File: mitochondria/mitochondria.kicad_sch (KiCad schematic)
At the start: 0 parts

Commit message: Started BMS with BQ77915 for 4S Battery design
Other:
- added sheet Battery Management (bms.kicad_sch)
- added sheet Connectors (conn.kicad_sch)
- added sheet Power Distribution (pd.kicad_sch)
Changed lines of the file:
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@@
 	(generator_version "9.0")
 	(paper "A4")
+	(sheet
+		(at 115.57 16.51)
+		(size 95.25 69.85)
+		(exclude_from_sim no)
+		(in_bom yes)
+		(on_board yes)
+		(dnp no)
+		(fields_autoplaced yes)
+		(stroke
+			(width 0.1524)
+			(type solid)
+		)
+		(fill
+			(color 0 0 0 0.0000)
+		)
+		(property "Sheetname" "Connectors"
+			(at 115.57 15.7984 0)
+			(effects
+				(font
+					(size 1.27 1.27)
+				)
+				(justify left bottom)
+			)
+		)
+		(property "Sheetfile" "conn.kicad_sch"
+			(at 115.57 86.9446 0)
+			(effects
+				(font
+					(size 1.27 1.27)
+				)
+				(justify left top)
+			)
+		)
+		(property "Field2" ""
+			(at 115.57 16.51 0)
+			(effects
+				(font
+					(size 1.27 1.27)
+				)
+				(hide yes)
+			)
+		)
+		(instances
+			(project "mitochondria"
+				(path "/d5881702-98ec-4aea-8d9c-3c163ba85aa3"
+					(page "3")
+				)
+			)
+		)
+	)
+	(sheet
+		(at 17.78 92.71)
+		(size 92.71 68.58)
+		(exclude_from_sim no)
+		(in_bom yes)
+		(on_board yes)
+		(dnp no)
+		(fields_autoplaced yes)
+		(stroke
+			(width 0.1524)
+			(type solid)
+		)
+		(fill
+			(color 0 0 0 0.0000)
+		)
+		(property "Sheetname" "Battery Management"
+			(at 17.78 91.9984 0)
+			(effects
+				(font
+					(size 1.27 1.27)
+				)
+				(justify left bottom)
+			)
+		)
+		(property "Sheetfile" "bms.kicad_sch"
+			(at 17.78 161.8746 0)
+			(effects
+				(font
+					(size 1.27 1.27)
+				)
+				(justify left top)
+			)
+		)
+		(pin "CELL_0" input
+			(at 110.49 100.33 0)
+			(effects
+				(font
+					(size 1.27 1.27)
+				)
+				(justify right)
+			)
+		)
+		(pin "CELL_1" input
+			(at 110.49 104.14 0)
+			(effects
+				(font
+					(size 1.27 1.27)
+				)
+				(justify right)
+			)
+		)
+		(pin "CELL_2" input
+			(at 110.49 107.95 0)
+			(effects
+				(font
+					(size 1.27 1.27)
+				)
+				(justify right)
+			)
+		)
+		(pin "CELL_3" input
+			(at 110.49 111.76 0)
+			(effects
+				(font
+					(size 1.27 1.27)
+				)
+				(justify right)
+			)
+		)
+		(instances
+			(project "mitochondria"
+				(path "/d5881702-98ec-4aea-8d9c-3c163ba85aa3"
+					(page "4")
+				)
+			)
+		)
+	)
+	(sheet
+		(at 17.78 16.51)
+		(size 92.71 69.85)
+		(exclude_from_sim no)
+		(in_bom yes)
+		(on_board yes)
+		(dnp no)
+		(fields_autoplaced yes)
+		(stroke
+			(width 0.1524)
+			(type solid)
+		)
+		(fill
+			(color 0 0 0 0.0000)
+		)
+		(property "Sheetname" "Power Distribution"
+			(at 17.78 15.7984 0)
+			(effects
+				(font
+					(size 1.27 1.27)
+				)
+				(justify left bottom)
+			)
+		)
+		(property "Sheetfile" "pd.kicad_sch"
+			(at 17.78 86.9446 0)
+			(effects
+				(font
+					(size 1.27 1.27)
+				)
+				(justify left top)
+			)
+		)
+		(property "Field2" ""
+			(at 17.78 16.51 0)
+			(effects
+				(font
+					(size 1.27 1.27)
+				)
+			)
+		)
+		(instances
+			(project "mitochondria"
+				(path "/d5881702-98ec-4aea-8d9c-3c163ba85aa3"
+					(page "2")
+				)
+			)
+		)
+	)
 	(sheet_instances
 		(path "/"

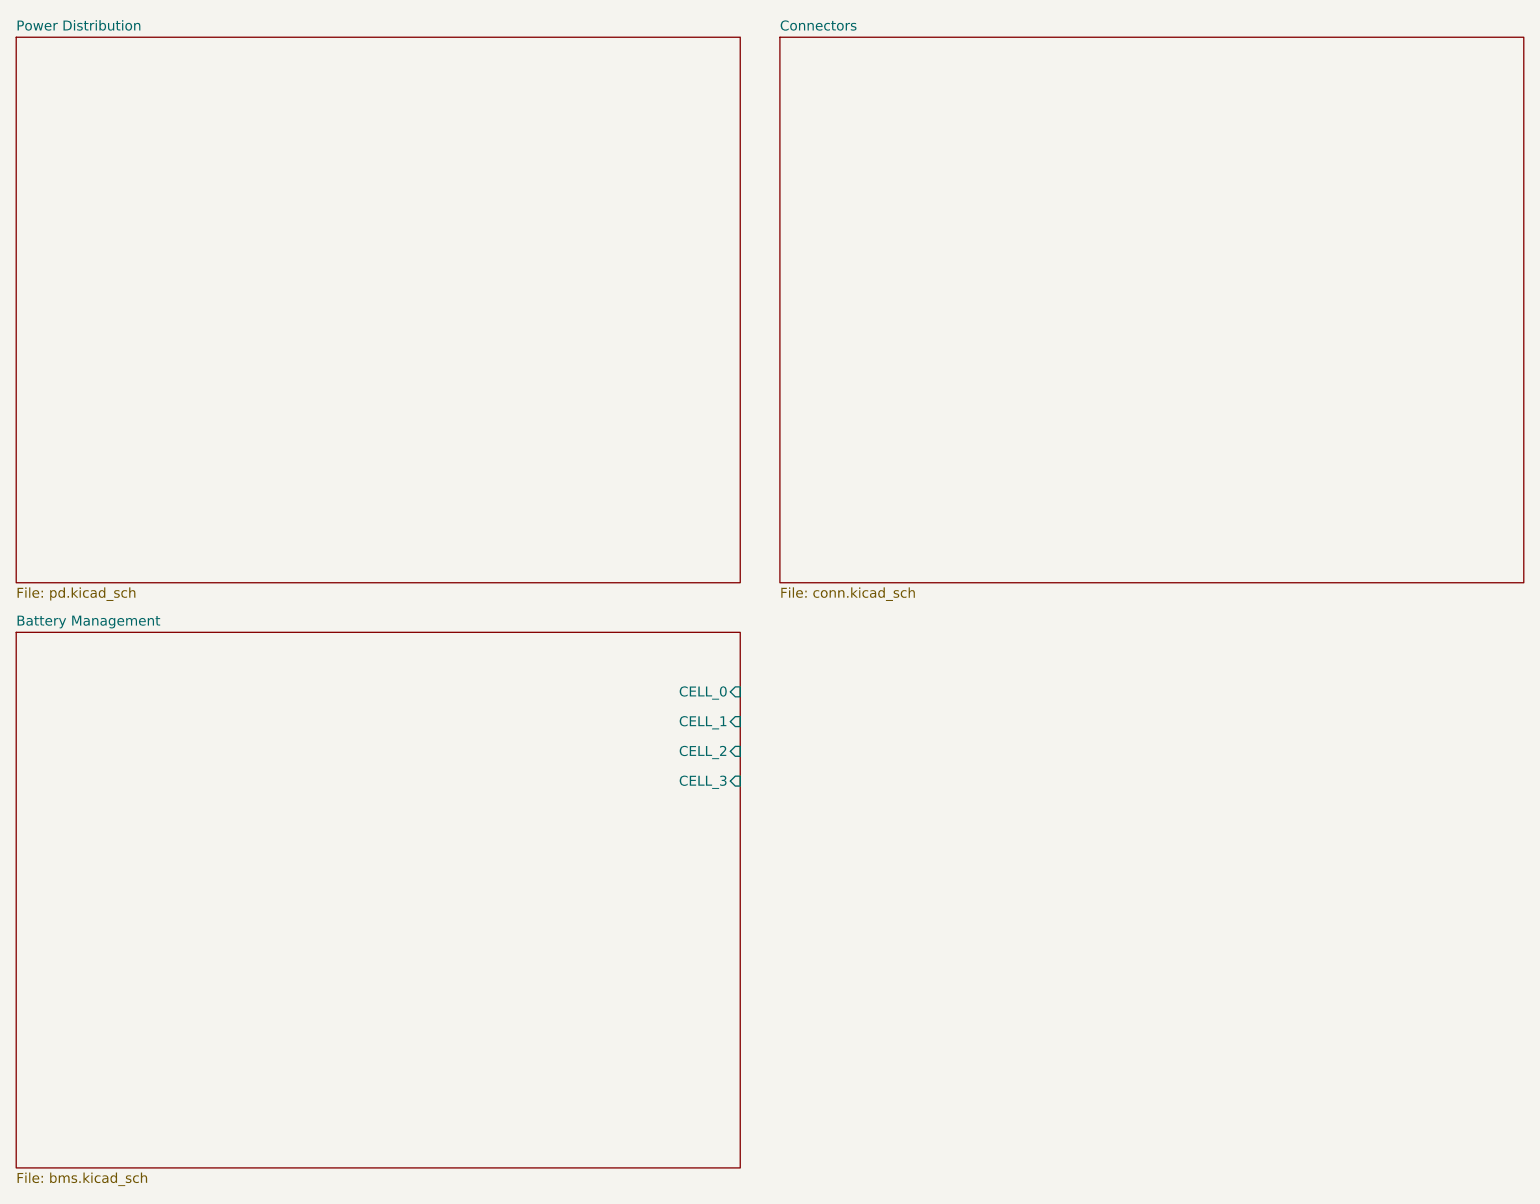
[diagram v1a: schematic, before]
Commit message: alpha 0.1.1: Unified versions, completed BMS + new subschematics
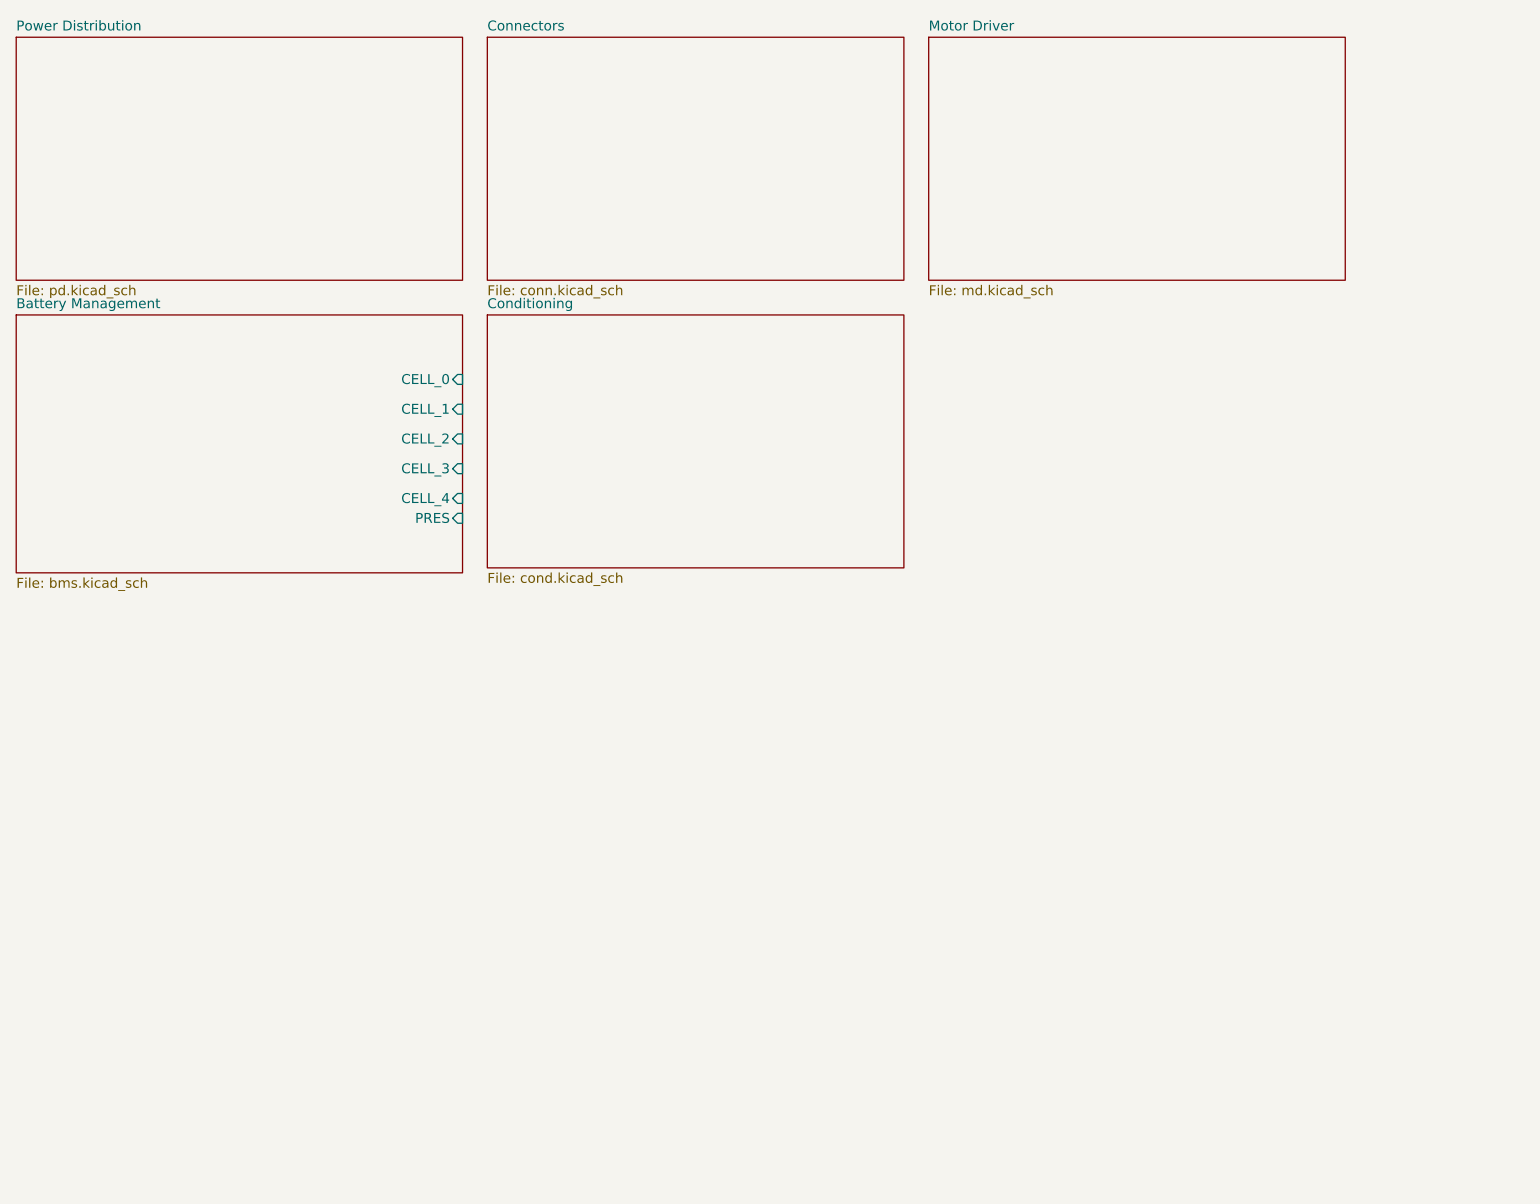
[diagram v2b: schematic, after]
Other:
- added sheet Conditioning (cond.kicad_sch)
- added sheet Motor Driver (md.kicad_sch)
- sheet Battery Management ports: added CELL_4, PRES; removed none
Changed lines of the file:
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@@
 	(paper "A4")
 	(sheet
-		(at 115.57 16.51)
-		(size 95.25 69.85)
+		(at 78.105 16.51)
+		(size 53.34 31.115)
 		(exclude_from_sim no)
 		(in_bom yes)
@@
 		)
 		(property "Sheetname" "Connectors"
-			(at 115.57 15.7984 0)
+			(at 78.105 15.7984 0)
 			(effects
 				(font
@@
 		)
 		(property "Sheetfile" "conn.kicad_sch"
-			(at 115.57 86.9446 0)
+			(at 78.105 48.2096 0)
 			(effects
 				(font
@@
 		)
 		(property "Field2" ""
-			(at 115.57 16.51 0)
+			(at 78.105 16.51 0)
 			(effects
 				(font
@@
 	)
 	(sheet
-		(at 17.78 92.71)
-		(size 92.71 68.58)
+		(at 17.78 52.07)
+		(size 57.15 33.02)
 		(exclude_from_sim no)
 		(in_bom yes)
@@
 		)
 		(property "Sheetname" "Battery Management"
-			(at 17.78 91.9984 0)
+			(at 17.78 51.3584 0)
 			(effects
 				(font
@@
 		)
 		(property "Sheetfile" "bms.kicad_sch"
-			(at 17.78 161.8746 0)
+			(at 17.78 85.6746 0)
 			(effects
 				(font
@@
 		)
 		(pin "CELL_0" input
-			(at 110.49 100.33 0)
+			(at 74.93 60.325 0)
 			(effects
 				(font
@@
 		)
 		(pin "CELL_1" input
-			(at 110.49 104.14 0)
+			(at 74.93 64.135 0)
 			(effects
 				(font
@@
 		)
 		(pin "CELL_2" input
-			(at 110.49 107.95 0)
+			(at 74.93 67.945 0)
 			(effects
 				(font
@@
 		)
 		(pin "CELL_3" input
-			(at 110.49 111.76 0)
+			(at 74.93 71.755 0)
+			(effects
+				(font
+					(size 1.27 1.27)
+				)
+				(justify right)
+			)
+		)
+		(pin "CELL_4" input
+			(at 74.93 75.565 0)
+			(effects
+				(font
+					(size 1.27 1.27)
+				)
+				(justify right)
+			)
+		)
+		(pin "PRES" input
+			(at 74.93 78.105 0)
 			(effects
 				(font
@@
 	)
 	(sheet
+		(at 78.105 52.07)
+		(size 53.34 32.385)
+		(exclude_from_sim no)
+		(in_bom yes)
+		(on_board yes)
+		(dnp no)
+		(fields_autoplaced yes)
+		(stroke
+			(width 0.1524)
+			(type solid)
+		)
+		(fill
+			(color 0 0 0 0.0000)
+		)
+		(property "Sheetname" "Conditioning"
+			(at 78.105 51.3584 0)
+			(effects
+				(font
+					(size 1.27 1.27)
+				)
+				(justify left bottom)
+			)
+		)
+		(property "Sheetfile" "cond.kicad_sch"
+			(at 78.105 85.0396 0)
+			(effects
+				(font
+					(size 1.27 1.27)
+				)
+				(justify left top)
+			)
+		)
+		(instances
+			(project "mitochondria"
+				(path "/d5881702-98ec-4aea-8d9c-3c163ba85aa3"
+					(page "5")
+				)
+			)
+		)
+	)
+	(sheet
+		(at 134.62 16.51)
+		(size 53.34 31.115)
+		(exclude_from_sim no)
+		(in_bom yes)
+		(on_board yes)
+		(dnp no)
+		(fields_autoplaced yes)
+		(stroke
+			(width 0.1524)
+			(type solid)
+		)
+		(fill
+			(color 0 0 0 0.0000)
+		)
+		(property "Sheetname" "Motor Driver"
+			(at 134.62 15.7984 0)
+			(effects
+				(font
+					(size 1.27 1.27)
+				)
+				(justify left bottom)
+			)
+		)
+		(property "Sheetfile" "md.kicad_sch"
+			(at 134.62 48.2096 0)
+			(effects
+				(font
+					(size 1.27 1.27)
+				)
+				(justify left top)
+			)
+		)
+		(property "Field2" ""
+			(at 134.62 16.51 0)
+			(effects
+				(font
+					(size 1.27 1.27)
+				)
+				(hide yes)
+			)
+		)
+		(instances
+			(project "mitochondria"
+				(path "/d5881702-98ec-4aea-8d9c-3c163ba85aa3"
+					(page "6")
+				)
+			)
+		)
+	)
+	(sheet
 		(at 17.78 16.51)
-		(size 92.71 69.85)
+		(size 57.15 31.115)
 		(exclude_from_sim no)
 		(in_bom yes)
@@
 		)
 		(property "Sheetfile" "pd.kicad_sch"
-			(at 17.78 86.9446 0)
-			(effects
-				(font
+			(at 17.78 48.2096 0)
+			(effects
+				(font
